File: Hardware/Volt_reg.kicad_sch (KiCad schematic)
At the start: 33 parts, among them Q2 BSZ025N04LS, Q3 BSZ025N04LS, U10 TPS55288QRPMRQ1, U8 INA219AxDCN

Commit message: Mega commit
Post review changes
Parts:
- removed R26: 2m, Resistor_SMD:R_2512_6332Metric_Pad1.40x3.35mm_HandSolder, symbol Device:R
- removed R29: 3.3k, Resistor_SMD:R_0402_1005Metric, symbol Device:R_Small
- added LED5: RED_LED, LED_SMD:LED_0402_1005Metric, symbol Device:LED_Small
- added R7: 3k, Resistor_SMD:R_0402_1005Metric, symbol Device:R_Small
- R48: value 50k -> 49.9k
- R51, R53: value 165k -> 110k
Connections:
- net ISN_2 is gone; now on net PyroPWR: R27.1, R49.2, U10.13 (ISN_1), U10.29 (ISN_2)
- net GND: now also LED5.1 (K)
- net PyroPWR: now also R7.1; no longer R28.1
- net VOUT_2: now also R28.1
- new net: LED5.2 (A), R7.2
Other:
- note added: "I2C current sensor uses the same resistor as the current sense for the buckboost"

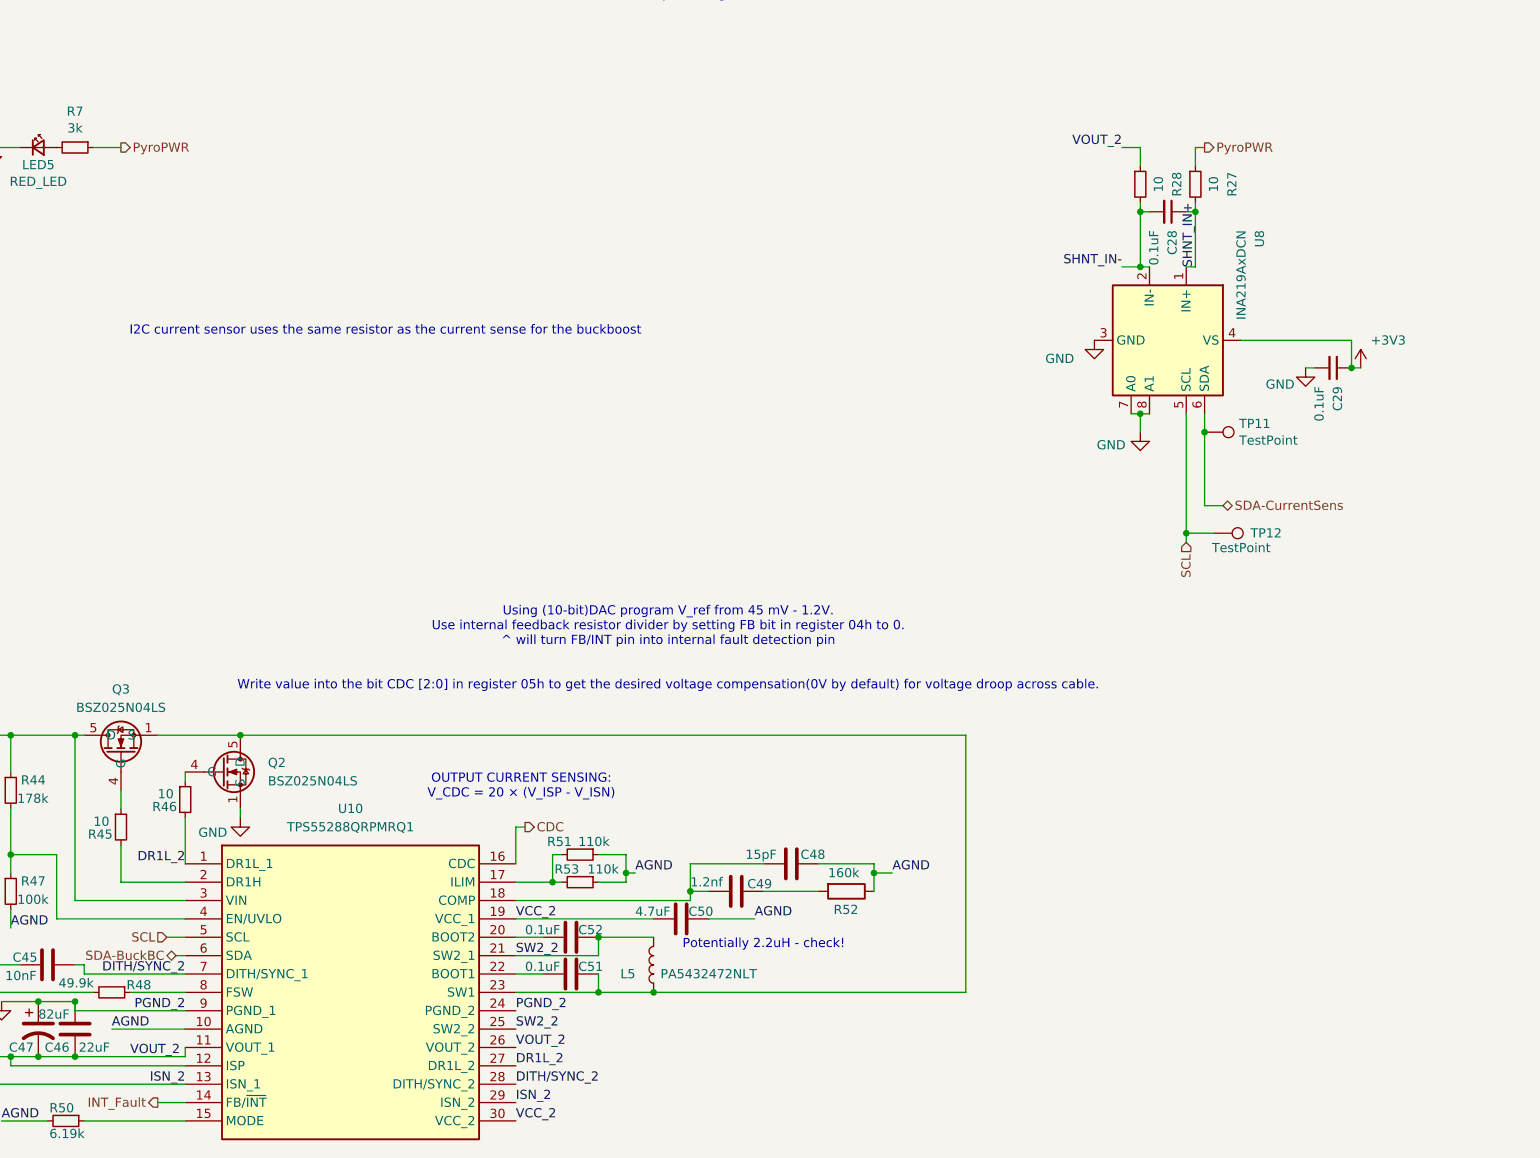
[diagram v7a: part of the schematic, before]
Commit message: V2 hardware changes
- Removed current sensor IC
- Removed photo sensor IC
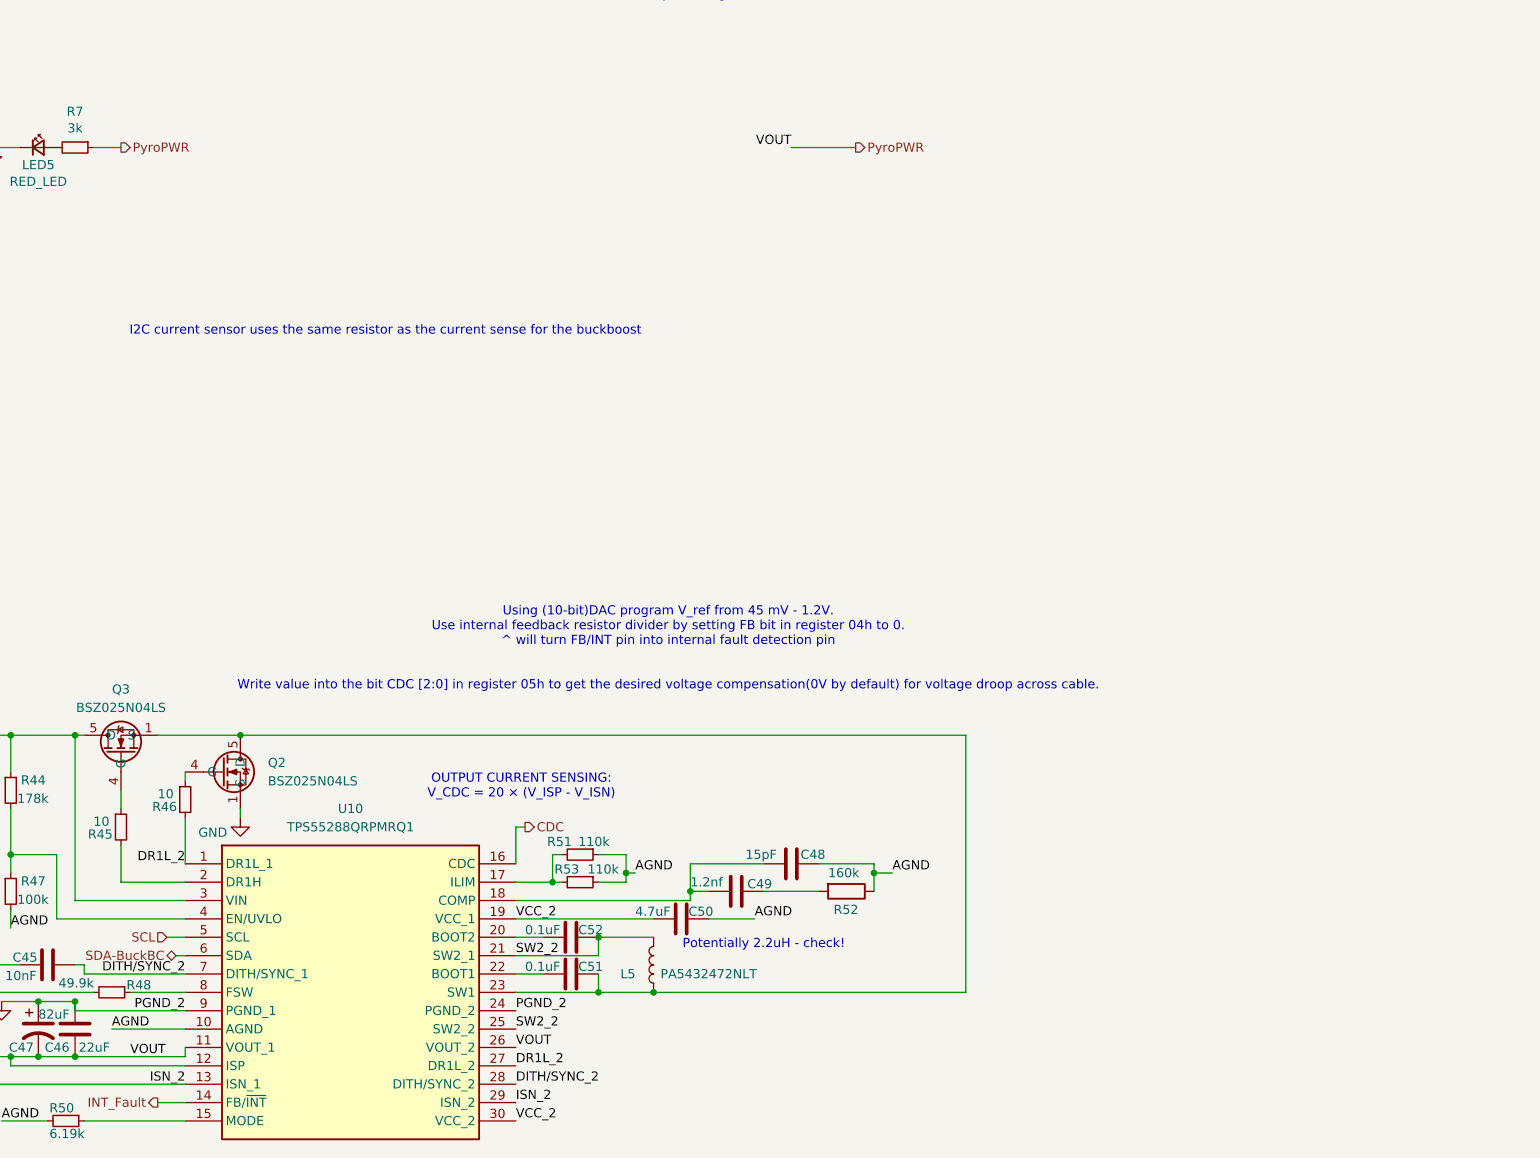
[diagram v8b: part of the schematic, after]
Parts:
- removed C28, C29: 0.1uF, Capacitor_SMD:C_0402_1005Metric, symbol Device:C_Small
- removed R27, R28: 10, Resistor_SMD:R_0402_1005Metric, symbol Device:R_Small
- removed TP11, TP12: TestPoint, TestPoint:TestPoint_Pad_D1.0mm, symbol Connector:TestPoint
- removed U8: INA219AxDCN, Package_TO_SOT_SMD:SOT-23-8, symbol Sensor_Energy:INA219AxDCN
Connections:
- net VOUT_2 is gone; now on net PyroPWR: C46.1, C47.2, R49.1, U10.11 (VOUT_1), U10.12 (ISP), U10.26 (VOUT_2)
